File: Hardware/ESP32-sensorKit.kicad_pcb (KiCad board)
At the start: 2 copper layers, 60 x 40 mm, 69 parts, among them P1 USB_C_Plug_USB2.0, Q1 S8050, Q2 S8050, Q3 S8050, Q4 S8050, Q5 S8050, U1 AMS1117-3.3, U2 AMS1117-3.3, U3 ESP32-WROOM-32D, U4 MPU-6050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

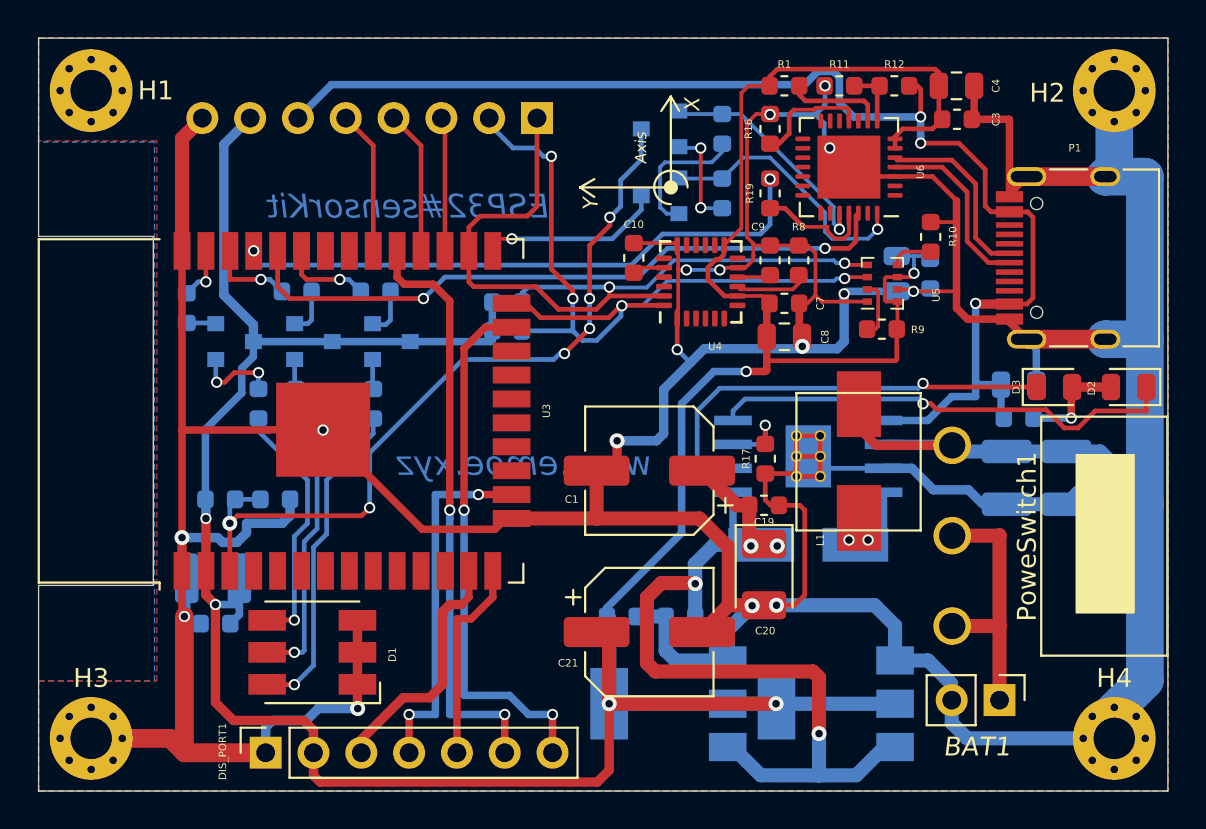
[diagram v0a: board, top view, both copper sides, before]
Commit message: Fix PCB bugs
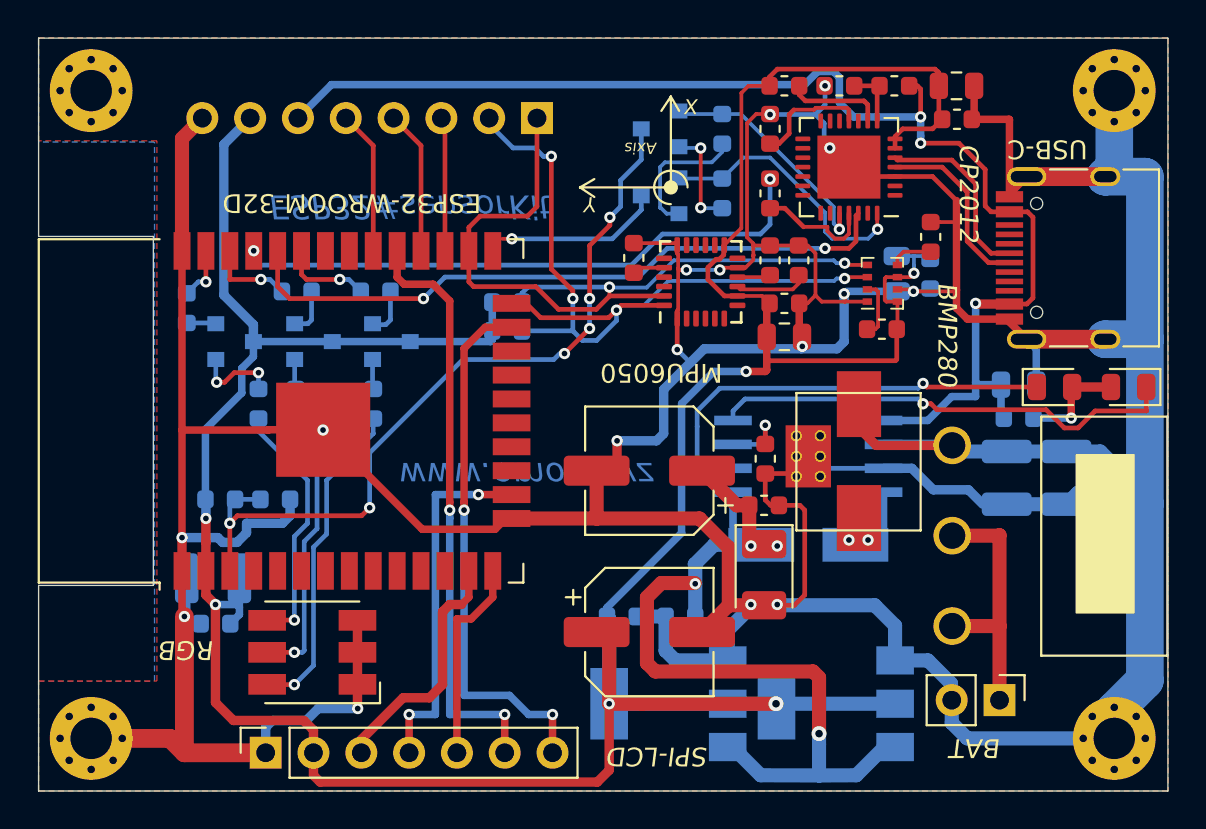
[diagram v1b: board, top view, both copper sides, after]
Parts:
- added REF**: KiCad-Logo2_5mm_SilkScreen, Symbol:KiCad-Logo2_5mm_SilkScreen, B.Cu at (129.0, 104.3)
- moved REF** 1.16 mm to (160.5, 104.3), turned to 0 degrees
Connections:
- U7 pad 10: (no net) -> GND
- U7 pad 9: (no net) -> GND
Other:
- board text added: "BAT"
- board text added: "BMP280"
- board text added: "CP2012"
- board text added: "ESP32-WROOM-32D"
- board text added: "MPU6050"
- board text added: "RGB"
- board text added: "SPI-LCD"
- board text added: "USB-C"
